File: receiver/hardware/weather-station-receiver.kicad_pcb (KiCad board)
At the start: 2 copper layers, 24.9 x 52.3 mm, 11 parts, among them J1 AntennaConnector, U1 RFM69, U2 PicoW, U3 APDS-9306-065, U4 BME280

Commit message: Finished Layout
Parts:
- added C4: 10uF, Capacitor_SMD:C_0805_2012Metric_Pad1.18x1.45mm_HandSolder, F.Cu at (170.3, 113.0)
- J1: value AntennaConnector -> Antenna
- U1: value RFM69 -> RFM69 915Mhz
- U2: footprint Weather_Station_Receiver:Pico SMD Headers -> Weather_Station_Receiver:Pico_SMD_Headers
- U3: value APDS-9306-065 -> Light Sensor
- moved C2 11.5 mm to (154.9, 89.3), turned to 180 degrees
- moved J1 8.24 mm to (166.4, 123.7), turned to 180 degrees
- moved U3 8.19 mm to (159.9, 89.8), turned to -90 degrees
- moved C1 6.66 mm to (158.0, 73.9)
- moved U1 5.50 mm to (159.0, 113.0)
- moved R2 4.98 mm to (160.2, 85.6), turned to 180 degrees
- moved R1 4.75 mm to (160.3, 82.9), turned to 180 degrees
- moved C3 4.01 mm to (161.5, 73.9)
- moved U4 3.66 mm to (160.0, 78.0), turned to -90 degrees
- moved R3 1.85 mm to (159.3, 93.7)
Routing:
- net /I2C0_SDA: track 29.7 -> 17.6 mm, vias 2 -> 3
- net /RFM69_INTR: track 0.00 -> 7.88 mm, vias 0 -> 1
- net /APDS_INTR: track 20.1 -> 12.6 mm
- net /RFM69_CS: track 23.5 -> 17.2 mm
- net Net-(J1-SIG): track 8.37 -> 2.25 mm
- net /SPI0_CLK: track 20.3 -> 15.7 mm
- net /SPI0_MOSI: track 16.9 -> 19.1 mm
- net GND: track 1.82 -> 0.00 mm, vias 0 -> 52
- net /RFM69_RESET: track 19.2 -> 20.8 mm
- net /SPI0_MISO: track 25.2 -> 25.9 mm
- net /I2C0_SCL: track 22.4 -> 22.8 mm, vias 3 -> 1
- net +3.3V: track 92.2 -> 91.8 mm, vias 1 -> 3
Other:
- board size 24.9 x 52.3 mm -> 25.1 x 58.2 mm

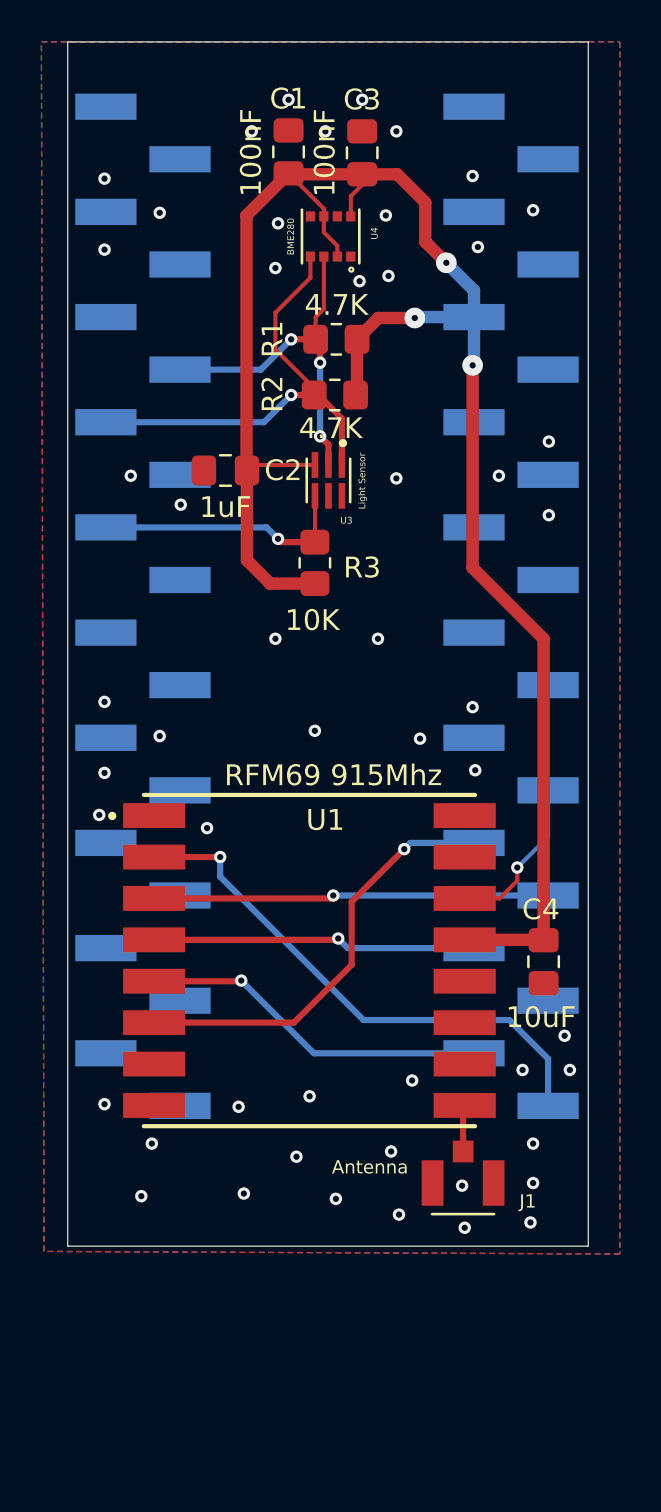
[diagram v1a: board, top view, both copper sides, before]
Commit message: Updated the weather stations components
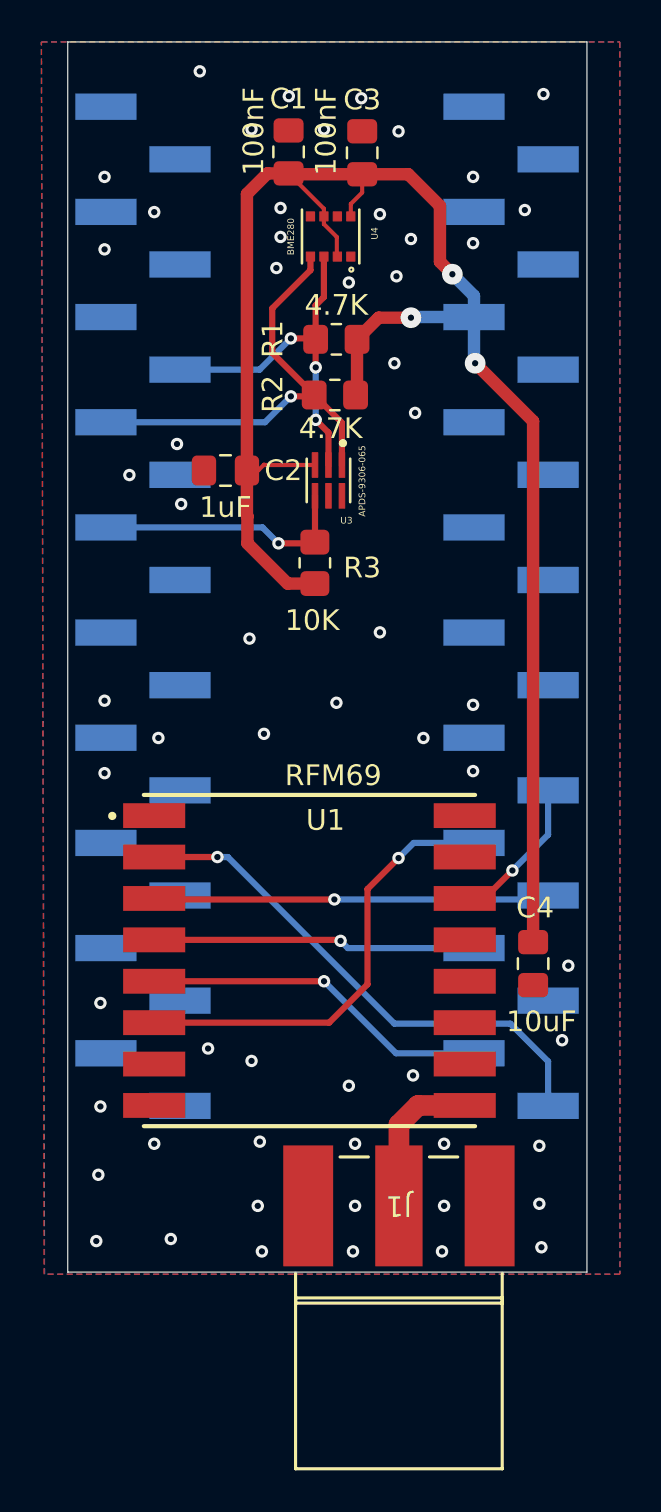
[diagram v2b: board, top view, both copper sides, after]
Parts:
- J1: value Antenna -> BoardAntennaConnector; footprint Weather_Station_Receiver:AntennaConnector -> Weather_Station_Receiver:PCB_Antenna
- U1: value RFM69 915Mhz -> RFM69
- U3: value Light Sensor -> APDS-9306-065
- moved J1 3.84 mm to (163.3, 126.0)
- moved C4 0.52 mm to (169.8, 113.1)
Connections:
- J1 pad 3: (no net) -> GND
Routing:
- net Net-(U1-ANT): track 2.25 -> 7.48 mm
- net +3.3V: track 91.8 -> 88.2 mm
- net /RFM69_RESET: track 20.8 -> 21.7 mm
- net /SPI0_MISO: track 25.9 -> 25.3 mm
- net GND: vias 52 -> 59
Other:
- board size 25.1 x 58.2 mm -> 25.1 x 59.4 mm
